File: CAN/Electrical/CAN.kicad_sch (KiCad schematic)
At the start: 21 parts, among them J3 Screw_Terminal_01x04, P1 USB_C_Plug_USB2.0, Q1 BSS214NW, Q2 BSS214NW, U1 AP2112K-3.3, U2 SN65HVD230, U5 ESP32-C3-MINI-1

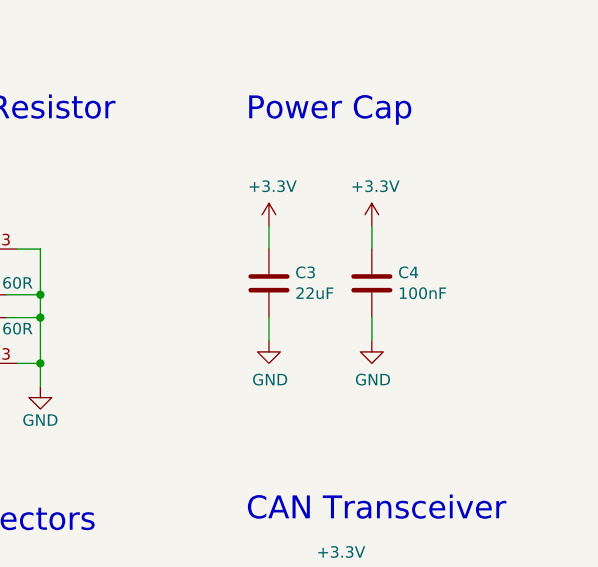
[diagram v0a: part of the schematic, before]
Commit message: Replaced Footprints
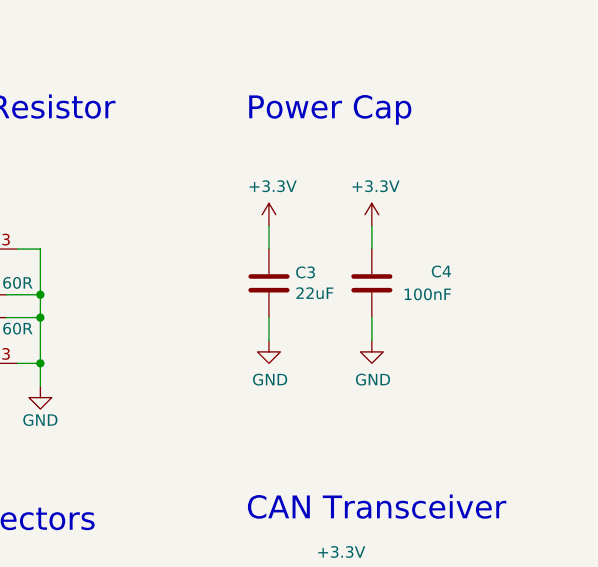
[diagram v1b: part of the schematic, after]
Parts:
- C1, C2, C3, C4: footprint Capacitor_SMD:C_0201_0603Metric_Pad0.64x0.40mm_HandSolder -> Capacitor_SMD:C_0603_1608Metric_Pad1.08x0.95mm_HandSolder
- R1: footprint Resistor_SMD:R_0201_0603Metric_Pad0.64x0.40mm_HandSolder -> Resistor_SMD:R_0603_1608Metric_Pad0.98x0.95mm_HandSolder
- R2, R3: footprint Resistor_SMD:R_0402_1005Metric_Pad0.72x0.64mm_HandSolder -> Resistor_SMD:R_0603_1608Metric_Pad0.98x0.95mm_HandSolder
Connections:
- net +3V3: now also C4.2; no longer C4.1
- net GND: now also C4.1; no longer C4.2
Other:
- moved on the sheet: C4
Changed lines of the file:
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@@
       (effects (font (size 1.27 1.27)) (justify left))
     )
-    (property "Footprint" "Capacitor_SMD:C_0201_0603Metric_Pad0.64x0.40mm_HandSolder" (at 81.28 39.37 0)
+    (property "Footprint" "Capacitor_SMD:C_0603_1608Metric_Pad1.08x0.95mm_HandSolder" (at 81.28 39.37 0)
       (effects (font (size 1.27 1.27)) hide)
     )
@@
       (effects (font (size 1.27 1.27)) (justify left))
     )
-    (property "Footprint" "Capacitor_SMD:C_0201_0603Metric_Pad0.64x0.40mm_HandSolder" (at 115.57 39.37 0)
+    (property "Footprint" "Capacitor_SMD:C_0603_1608Metric_Pad1.08x0.95mm_HandSolder" (at 115.57 39.37 0)
       (effects (font (size 1.27 1.27)) hide)
     )
@@
       (effects (font (size 1.27 1.27)) (justify left))
     )
-    (property "Footprint" "Capacitor_SMD:C_0201_0603Metric_Pad0.64x0.40mm_HandSolder" (at 239.7252 96.52 0)
+    (property "Footprint" "Capacitor_SMD:C_0603_1608Metric_Pad1.08x0.95mm_HandSolder" (at 239.7252 96.52 0)
       (effects (font (size 1.27 1.27)) hide)
     )
@@
       (effects (font (size 1.27 1.27)))
     )
-    (property "Footprint" "Resistor_SMD:R_0402_1005Metric_Pad0.72x0.64mm_HandSolder" (at 205.74 95.758 90)
+    (property "Footprint" "Resistor_SMD:R_0603_1608Metric_Pad0.98x0.95mm_HandSolder" (at 205.74 95.758 90)
       (effects (font (size 1.27 1.27)) hide)
     )
@@
       (effects (font (size 1.27 1.27)))
     )
-    (property "Footprint" "Resistor_SMD:R_0201_0603Metric_Pad0.64x0.40mm_HandSolder" (at 60.96 38.608 90)
+    (property "Footprint" "Resistor_SMD:R_0603_1608Metric_Pad0.98x0.95mm_HandSolder" (at 60.96 38.608 90)
       (effects (font (size 1.27 1.27)) hide)
     )
@@
       (effects (font (size 1.27 1.27)))
     )
-    (property "Footprint" "Resistor_SMD:R_0402_1005Metric_Pad0.72x0.64mm_HandSolder" (at 205.74 98.298 90)
+    (property "Footprint" "Resistor_SMD:R_0603_1608Metric_Pad0.98x0.95mm_HandSolder" (at 205.74 98.298 90)
       (effects (font (size 1.27 1.27)) hide)
     )
@@
     )
   )
-  (symbol (lib_id "Device:C") (at 250.19 92.71 0) (unit 1)
-    (in_bom yes) (on_board yes) (dnp no)
-    (property "Reference" "C4" (at 253.111 91.5416 0)
-      (effects (font (size 1.27 1.27)) (justify left))
-    )
-    (property "Value" "100nF" (at 253.111 93.853 0)
-      (effects (font (size 1.27 1.27)) (justify left))
-    )
-    (property "Footprint" "Capacitor_SMD:C_0201_0603Metric_Pad0.64x0.40mm_HandSolder" (at 251.1552 96.52 0)
-      (effects (font (size 1.27 1.27)) hide)
-    )
+  (symbol (lib_id "Device:C") (at 250.19 92.71 180) (unit 1)
+    (in_bom yes) (on_board yes) (dnp no)
+    (property "Reference" "C4" (at 259.08 91.44 0)
+      (effects (font (size 1.27 1.27)) (justify left))
+    )
+    (property "Value" "100nF" (at 259.08 93.98 0)
+      (effects (font (size 1.27 1.27)) (justify left))
+    )
+    (property "Footprint" "Capacitor_SMD:C_0603_1608Metric_Pad1.08x0.95mm_HandSolder" (at 249.2248 88.9 0)
+      (effects (font (size 1.27 1.27)) hide)
+    )

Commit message: Fixed S
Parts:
- removed H3: MountingHole, MountingHole:MountingHole_2.2mm_M2, symbol Mechanical:MountingHole
- renumbered J3 to J1
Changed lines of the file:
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@@
   (symbol (lib_id "Connector:Screw_Terminal_01x04") (at 198.12 140.97 180) (unit 1)
     (in_bom yes) (on_board yes) (dnp no) (fields_autoplaced)
-    (property "Reference" "J3" (at 198.12 129.54 0)
+    (property "Reference" "J1" (at 198.12 129.54 0)
       (effects (font (size 1.27 1.27)))
     )
@@
       (project "CAN"
         (path "/21020eba-b649-4135-9bee-384d0a5cab58"
-          (reference "J3") (unit 1)
+          (reference "J1") (unit 1)
         )
       )
@@
         )
       )
-    )
-  )
-  (symbol (lib_id "Mechanical:MountingHole") (at 189.23 21.59 0) (unit 1)
-    (in_bom yes) (on_board yes) (dnp no)
-    (property "Reference" "H3" (at 191.77 20.3454 0)
-      (effects (font (size 1.27 1.27)) (justify left))
-    )
-    (property "Value" "MountingHole" (at 191.77 22.6568 0)
-      (effects (font (size 1.27 1.27)) (justify left))
-    )
-    (property "Footprint" "MountingHole:MountingHole_2.2mm_M2" (at 189.23 21.59 0)
-      (effects (font (size 1.27 1.27)) hide)
-    )
-    (property "Datasheet" "~" (at 189.23 21.59 0)
-      (effects (font (size 1.27 1.27)) hide)
-    )
-    (instances
-      (project "CAN"
-        (path "/21020eba-b649-4135-9bee-384d0a5cab58"
-          (reference "H3") (unit 1)
-        )
-      )

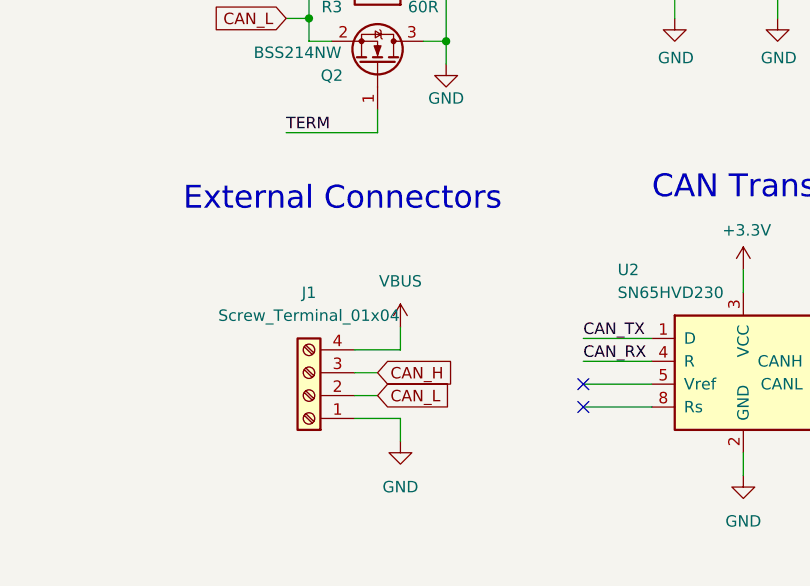
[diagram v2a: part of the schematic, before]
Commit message: Replaced Screw terminal with pin socket
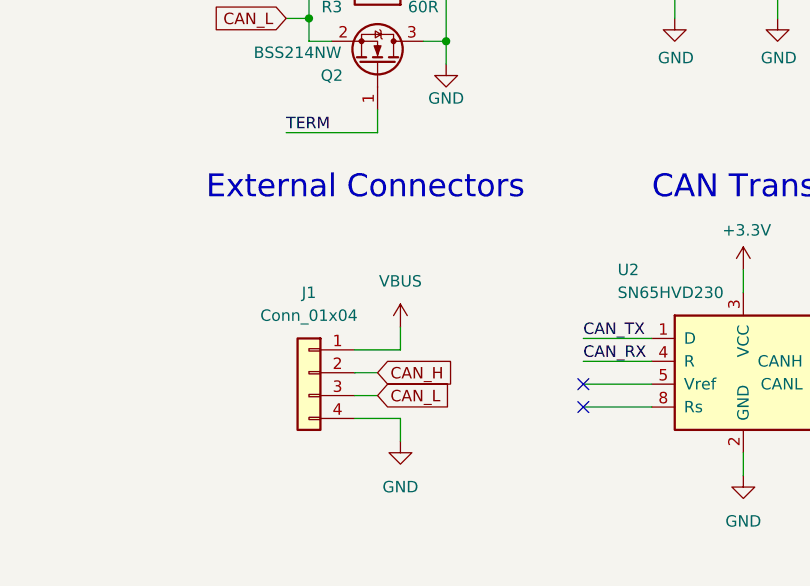
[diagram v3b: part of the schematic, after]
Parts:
- removed J1: Screw_Terminal_01x04, Connector_PinHeader_2.54mm:PinHeader_1x04_P2.54mm_Horizontal, symbol Connector:Screw_Terminal_01x04
- added J1: Conn_01x04, Connector_PinSocket_2.54mm:PinSocket_1x04_P2.54mm_Horizontal, symbol Connector_Generic:Conn_01x04
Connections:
- net CAN_H: now also J1.2 (Pin_2)
- net CAN_L: now also J1.3 (Pin_3)
- net GND: now also J1.4 (Pin_4)
- net VBUS: now also J1.1 (Pin_1)
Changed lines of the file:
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@@
     (effects (font (size 2.54 2.54)) (justify left bottom))
   )
-  (text "External Connectors" (at 184.15 120.65 0)
+  (text "External Connectors" (at 186.69 119.38 0)
     (effects (font (size 2.54 2.54)) (justify left bottom))
   )
@@
     )
   )
-  (symbol (lib_id "Connector:Screw_Terminal_01x04") (at 198.12 140.97 180) (unit 1)
+  (symbol (lib_id "Connector_Generic:Conn_01x04") (at 198.12 138.43 0) (mirror y) (unit 1)
     (in_bom yes) (on_board yes) (dnp no) (fields_autoplaced)
     (property "Reference" "J1" (at 198.12 129.54 0)
       (effects (font (size 1.27 1.27)))
     )
-    (property "Value" "Screw_Terminal_01x04" (at 198.12 132.08 0)
-      (effects (font (size 1.27 1.27)))
-    )
-    (property "Footprint" "Connector_PinHeader_2.54mm:PinHeader_1x04_P2.54mm_Horizontal" (at 198.12 140.97 0)
-      (effects (font (size 1.27 1.27)) hide)
-    )
-    (property "Datasheet" "~" (at 198.12 140.97 0)
-      (effects (font (size 1.27 1.27)) hide)
-    )
+    (property "Value" "Conn_01x04" (at 198.12 132.08 0)
+      (effects (font (size 1.27 1.27)))
+    )
+    (property "Footprint" "Connector_PinSocket_2.54mm:PinSocket_1x04_P2.54mm_Horizontal" (at 198.12 138.43 0)
+      (effects (font (size 1.27 1.27)) hide)
+    )
+    (property "Datasheet" "~" (at 198.12 138.43 0)
+      (effects (font (size 1.27 1.27)) hide)
+    )

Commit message: Updated PCB
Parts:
- added TP5, TP6, TP7, TP8: TestPoint, TestPoint:TestPoint_Pad_1.5x1.5mm, symbol Connector:TestPoint
- C1, C2, C3, C4: footprint Capacitor_SMD:C_0603_1608Metric_Pad1.08x0.95mm_HandSolder -> Capacitor_SMD:C_0805_2012Metric_Pad1.18x1.45mm_HandSolder
- R1: footprint Resistor_SMD:R_0603_1608Metric_Pad0.98x0.95mm_HandSolder -> Resistor_SMD:R_0805_2012Metric_Pad1.20x1.40mm_HandSolder
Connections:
- net +3V3 is gone; now on net +3.3V: C2.1, C3.1, C4.2, U1.5 (VOUT), U2.3 (VCC)
- net +3.3V: now also U5.8 (EN/CHIP_PU), TP6.1, TP8.1
- net VBUS: now also TP5.1, TP7.1
- no-connect marks 12 -> 11
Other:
- moved on the sheet: TP1, TP2, TP3, TP4

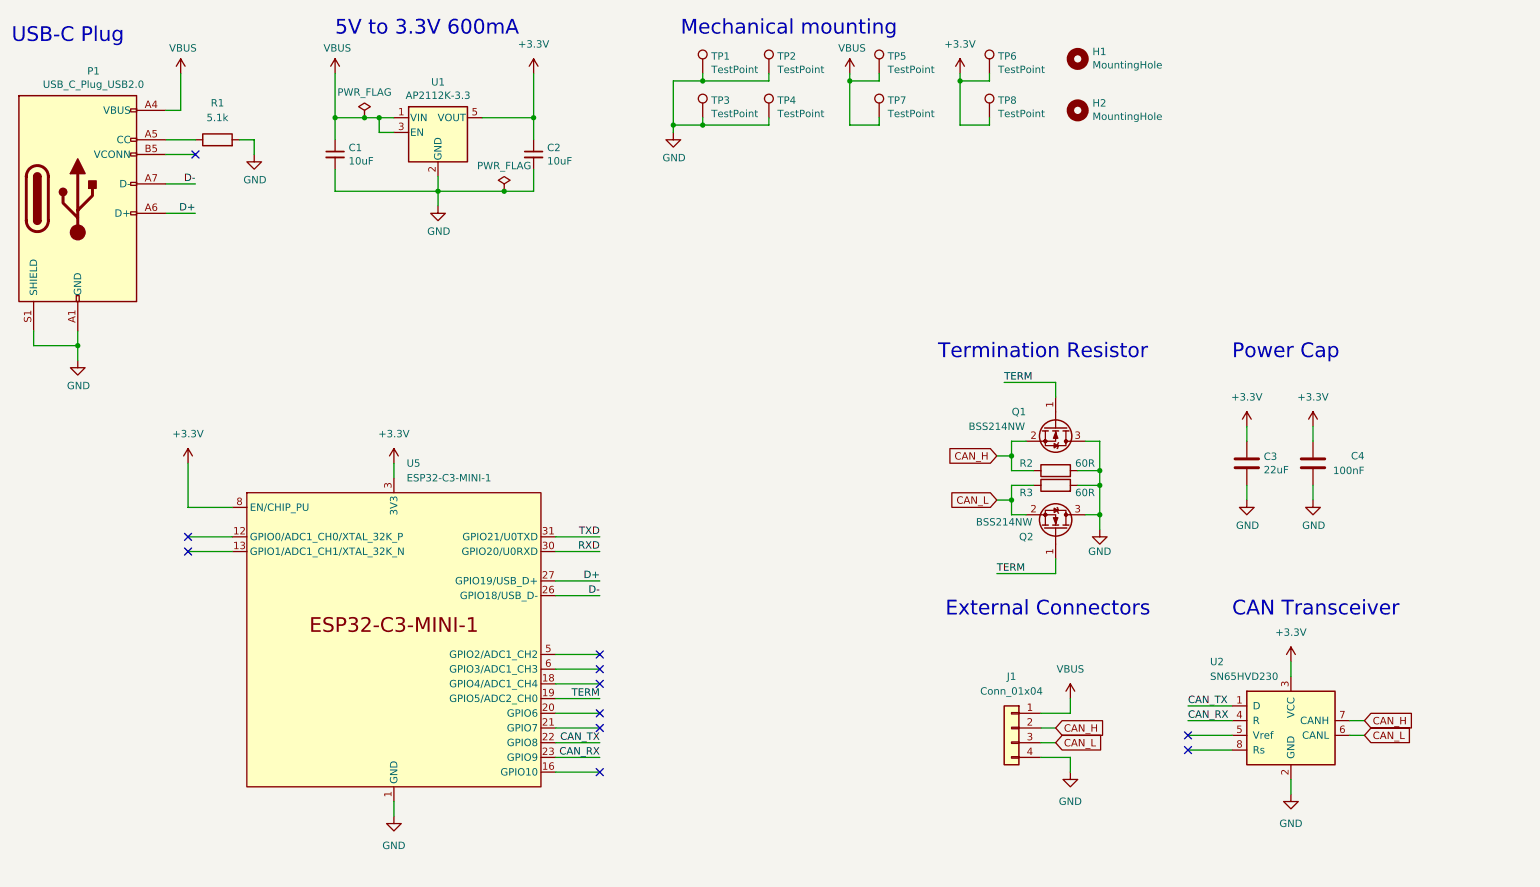
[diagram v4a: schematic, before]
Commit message: Updated Schematic
Added Volatage output Selection
Added PullUp resistor & PullDown capacitor to EN
Added PullUp resistor to GPIO2
Updated Power cap capacitors
Added reset button
Changed Tespoints 7 & 8 to TX and RX
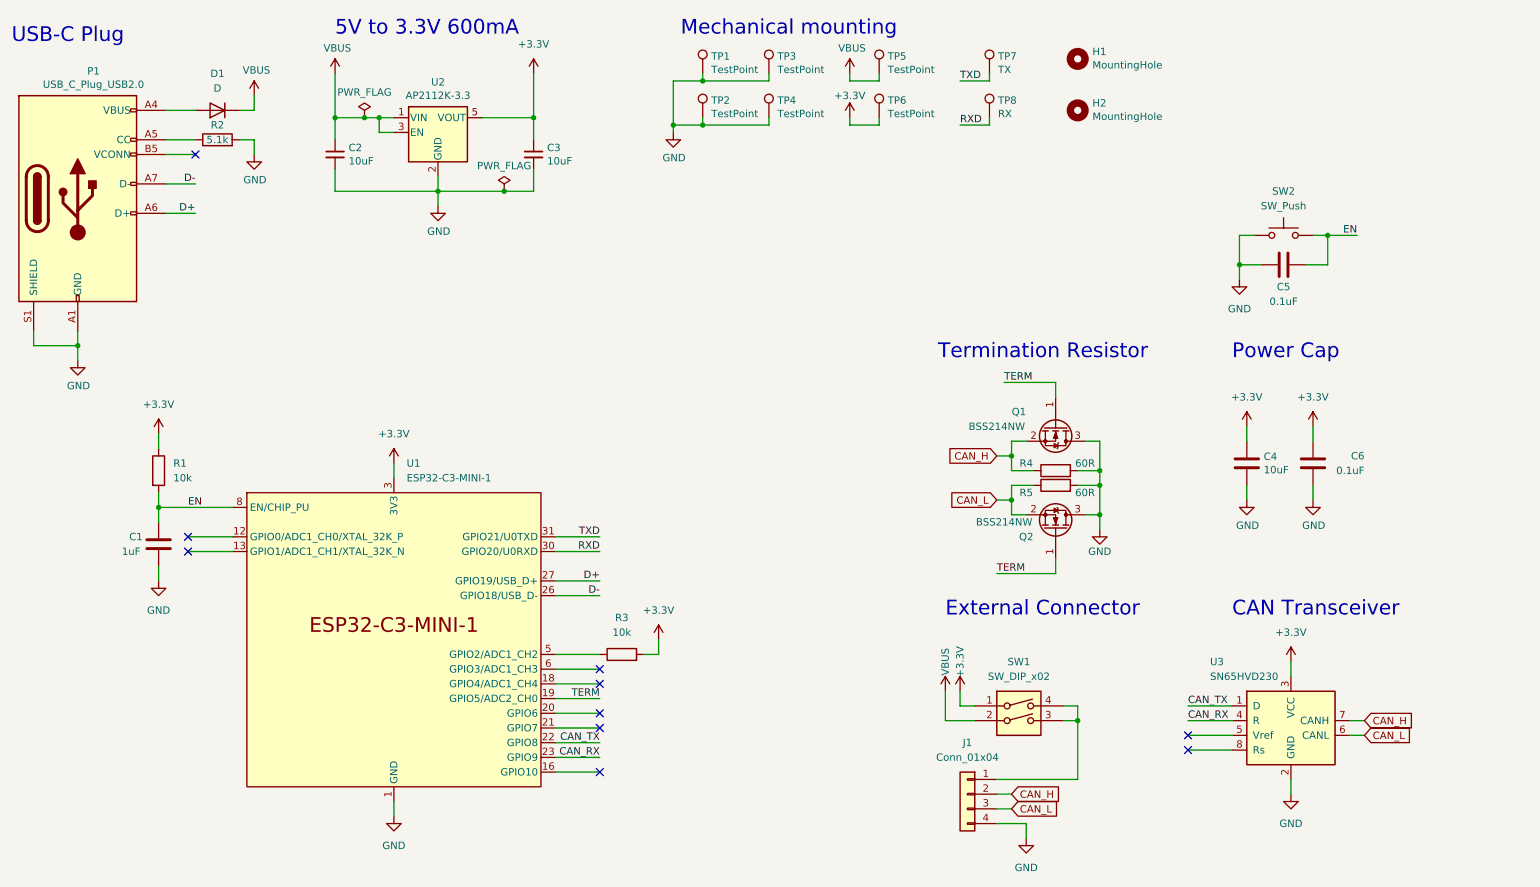
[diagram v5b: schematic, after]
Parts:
- added C1: 1uF, Capacitor_SMD:C_0805_2012Metric_Pad1.18x1.45mm_HandSolder, symbol Device:C
- added C5: 0.1uF, Capacitor_SMD:C_0805_2012Metric_Pad1.18x1.45mm_HandSolder, symbol Device:C
- added D1: D, Diode_SMD:D_0805_2012Metric_Pad1.15x1.40mm_HandSolder, symbol Device:D
- added R1, R3: 10k, Resistor_SMD:R_0805_2012Metric_Pad1.20x1.40mm_HandSolder, symbol Device:R
- added SW1: SW_DIP_x02, Button_Switch_SMD:SW_DIP_SPSTx02_Slide_Copal_CHS-02A_W5.08mm_P1.27mm_JPin, symbol Switch:SW_DIP_x02
- added SW2: SW_Push, Button_Switch_SMD:SW_SPST_B3U-3000P, symbol Switch:SW_Push
- C4: renamed from C3; value 22uF -> 10uF
- C6: renamed from C4; value 100nF -> 0.1uF
- P1: footprint (none) -> Expansion_Card:USB_C_Plug_Molex_105444
- R4: renamed from R2; footprint Resistor_SMD:R_0603_1608Metric_Pad0.98x0.95mm_HandSolder -> Resistor_SMD:R_0805_2012Metric_Pad1.20x1.40mm_HandSolder
- R5: renamed from R3; footprint Resistor_SMD:R_0603_1608Metric_Pad0.98x0.95mm_HandSolder -> Resistor_SMD:R_0805_2012Metric_Pad1.20x1.40mm_HandSolder
- TP7: value TestPoint -> TX
- TP8: value TestPoint -> RX
- renumbered C1 to C2, C2 to C3, R1 to R2, TP3 to TP2, TP2 to TP3, U5 to U1, U1 to U2, U2 to U3
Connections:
- net +3.3V: now also R1.1, R3.2, SW1.1; no longer TP8.1, U1.8 (EN/CHIP_PU)
- net GND: now also C1.2, C5.1, SW2.1
- net RXD: now also TP8.1
- net TXD: now also TP7.1
- net VBUS: now also D1.1 (K), SW1.2; no longer J1.1 (Pin_1), P1.A4 (VBUS), P1.A9 (VBUS), P1.B4 (VBUS), P1.B9 (VBUS), TP7.1
- net at U1.5 (GPIO2/ADC1_CH2): now also R3.1
- new net: D1.2 (A), P1.A4 (VBUS), P1.A9 (VBUS), P1.B4 (VBUS), P1.B9 (VBUS)
- new net: J1.1 (Pin_1), SW1.3, SW1.4
- new net EN: C1.1, C5.2, R1.2, SW2.2, U1.8 (EN/CHIP_PU)
- no-connect marks 11 -> 10
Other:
- note added: "External Connector"
- note removed: "External Connectors"
- moved on the sheet: J1, TP6

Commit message: Updated project
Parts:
- TP5: value TestPoint -> VBUS
- TP6: value TestPoint -> 3.3V
- renumbered SW2 to SW1, SW1 to SW2
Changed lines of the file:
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@@
       (effects (font (size 1.27 1.27)) (justify left))
     )
-    (property "Value" "TestPoint" (at 176.7332 24.7142 0)
+    (property "Value" "VBUS" (at 176.7332 24.7142 0)
       (effects (font (size 1.27 1.27)) (justify left))
     )
@@
   (symbol (lib_id "Switch:SW_DIP_x02") (at 199.39 137.16 0) (unit 1)
     (in_bom yes) (on_board yes) (dnp no) (fields_autoplaced)
-    (property "Reference" "SW1" (at 199.39 127 0)
+    (property "Reference" "SW2" (at 199.39 127 0)
       (effects (font (size 1.27 1.27)))
     )
@@
       (project "CAN"
         (path "/21020eba-b649-4135-9bee-384d0a5cab58"
-          (reference "SW1") (unit 1)
+          (reference "SW2") (unit 1)
         )
       )
@@
       (effects (font (size 1.27 1.27)) (justify left))
     )
-    (property "Value" "TestPoint" (at 176.7332 32.3342 0)
+    (property "Value" "3.3V" (at 176.7332 32.3342 0)
       (effects (font (size 1.27 1.27)) (justify left))
     )
@@
   (symbol (lib_id "Switch:SW_Push") (at 245.11 53.34 0) (unit 1)
     (in_bom yes) (on_board yes) (dnp no) (fields_autoplaced)
-    (property "Reference" "SW2" (at 245.11 45.72 0)
+    (property "Reference" "SW1" (at 245.11 45.72 0)
       (effects (font (size 1.27 1.27)))
     )
@@
       (project "CAN"
         (path "/21020eba-b649-4135-9bee-384d0a5cab58"
-          (reference "SW2") (unit 1)
-        )
-      )
+          (reference "SW1") (unit 1)
+        )
+      )

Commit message: Updated Schematic
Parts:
- removed D1: D, Diode_SMD:D_0805_2012Metric_Pad1.15x1.40mm_HandSolder, symbol Device:D
- removed J1: Conn_01x04, Connector_PinSocket_2.54mm:PinSocket_1x04_P2.54mm_Horizontal, symbol Connector_Generic:Conn_01x04
- removed Q1, Q2: BSS214NW, Package_TO_SOT_SMD:SOT-323_SC-70, symbol Transistor_FET:BSS214NW
- removed R4: 60R, Resistor_SMD:R_0805_2012Metric_Pad1.20x1.40mm_HandSolder, symbol Device:R
- removed SW2: SW_DIP_x02, Button_Switch_SMD:SW_DIP_SPSTx02_Slide_Copal_CHS-02A_W5.08mm_P1.27mm_JPin, symbol Switch:SW_DIP_x02
- added D1: D_Schottky, Diode_SMD:D_0805_2012Metric_Pad1.15x1.40mm_HandSolder, symbol Device:D_Schottky
- added D2: LED, LED_SMD:LED_0805_2012Metric_Pad1.15x1.40mm_HandSolder, symbol Device:LED
- added J1: Conn_01x05, Connector_PinSocket_2.54mm:PinSocket_1x05_P2.54mm_Horizontal, symbol Connector_Generic:Conn_01x05
- added R3: 5.1k, Resistor_SMD:R_0805_2012Metric_Pad1.20x1.40mm_HandSolder, symbol Device:R
- added R6: 10k, Resistor_SMD:R_0805_2012Metric_Pad1.20x1.40mm_HandSolder, symbol Device:R
- added R7: 120R, Resistor_SMD:R_0805_2012Metric_Pad1.20x1.40mm_HandSolder, symbol Device:R
- added U5: FODM217D, Package_SO:SOP-4_4.4x2.6mm_P1.27mm, symbol Isolator:FODM217D
- R5: value 60R -> 5.1k
- SW1: value SW_Push -> Reset
- renumbered R3 to R4
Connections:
- net CAN_H: now also J1.3 (Pin_3), U5.1
- net CAN_L: now also J1.4 (Pin_4), R7.1; no longer R5.1
- net GND: now also D2.1 (K), J1.5 (Pin_5), R3.2, R6.1, U5.3; no longer R5.2
- net TERM: now also U5.4
- net VBUS: now also R5.1, D1.1 (K), J1.2 (Pin_2)
- net at P1.A4 (VBUS), P1.A9 (VBUS), P1.B4 (VBUS)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: now also D1.2 (A)
- net at P1.B5 (VCONN): now also R3.1
- net at U3.8 (Rs): now also R6.2
- net GPIO6: now reaches U1.20 (GPIO6)
- net GPIO6: now also J1.1 (Pin_1)
- new net: D2.2 (A), R5.2
- new net: R7.2, U5.2
- no-connect marks 10 -> 7
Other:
- note added: "Reset Button"
- note removed: "Termination Resistor"
- moved on the sheet: C4, C5, C6, SW1, U3
